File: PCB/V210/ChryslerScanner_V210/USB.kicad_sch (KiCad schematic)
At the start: 11 parts

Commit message: Completed schematic.
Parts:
- gave numbers to parts that had none: 11
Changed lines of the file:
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@@
   (symbol (lib_id "Device:R") (at 180.34 62.23 0) (unit 1)
     (in_bom yes) (on_board yes) (fields_autoplaced)
-    (property "Reference" "R?" (id 0) (at 182.88 60.9599 0)
+    (property "Reference" "R12" (id 0) (at 182.88 60.9599 0)
       (effects (font (size 1.27 1.27)) (justify left))
     )
@@
   (symbol (lib_id "power:PWR_FLAG") (at 88.9 83.82 0) (unit 1)
     (in_bom yes) (on_board yes) (fields_autoplaced)
-    (property "Reference" "#FLG?" (id 0) (at 88.9 81.915 0)
+    (property "Reference" "#FLG01" (id 0) (at 88.9 81.915 0)
       (effects (font (size 1.27 1.27)) hide)
     )
@@
   (symbol (lib_id "power:+3V3") (at 205.74 50.8 0) (unit 1)
     (in_bom yes) (on_board yes) (fields_autoplaced)
-    (property "Reference" "#PWR?" (id 0) (at 205.74 54.61 0)
+    (property "Reference" "#PWR025" (id 0) (at 205.74 54.61 0)
       (effects (font (size 1.27 1.27)) hide)
     )
@@
   (symbol (lib_id "power:+5V") (at 87.63 59.69 0) (unit 1)
     (in_bom yes) (on_board yes) (fields_autoplaced)
-    (property "Reference" "#PWR?" (id 0) (at 87.63 63.5 0)
+    (property "Reference" "#PWR017" (id 0) (at 87.63 63.5 0)
       (effects (font (size 1.27 1.27)) hide)
     )
@@
   (symbol (lib_id "power:VBUS") (at 180.34 50.8 0) (unit 1)
     (in_bom yes) (on_board yes) (fields_autoplaced)
-    (property "Reference" "#PWR?" (id 0) (at 180.34 54.61 0)
+    (property "Reference" "#PWR023" (id 0) (at 180.34 54.61 0)
       (effects (font (size 1.27 1.27)) hide)
     )
@@
   (symbol (lib_id "Interface_USB:CP2102N-Axx-xQFN28") (at 208.28 97.79 0) (unit 1)
     (in_bom yes) (on_board yes) (fields_autoplaced)
-    (property "Reference" "U?" (id 0) (at 210.2994 130.81 0)
+    (property "Reference" "U4" (id 0) (at 210.2994 130.81 0)
       (effects (font (size 1.27 1.27)) (justify left))
     )
@@
   (symbol (lib_id "power:VBUS") (at 120.65 85.09 0) (unit 1)
     (in_bom yes) (on_board yes) (fields_autoplaced)
-    (property "Reference" "#PWR?" (id 0) (at 120.65 88.9 0)
+    (property "Reference" "#PWR019" (id 0) (at 120.65 88.9 0)
       (effects (font (size 1.27 1.27)) hide)
     )
@@
   (symbol (lib_id "power:GND") (at 120.65 139.7 0) (unit 1)
     (in_bom yes) (on_board yes) (fields_autoplaced)
-    (property "Reference" "#PWR?" (id 0) (at 120.65 146.05 0)
+    (property "Reference" "#PWR020" (id 0) (at 120.65 146.05 0)
       (effects (font (size 1.27 1.27)) hide)
     )
@@
   (symbol (lib_id "power:+3V3") (at 165.1 50.8 0) (unit 1)
     (in_bom yes) (on_board yes) (fields_autoplaced)
-    (property "Reference" "#PWR?" (id 0) (at 165.1 54.61 0)
+    (property "Reference" "#PWR021" (id 0) (at 165.1 54.61 0)
       (effects (font (size 1.27 1.27)) hide)
     )
@@
   (symbol (lib_id "Device:R") (at 180.34 76.2 0) (unit 1)
     (in_bom yes) (on_board yes) (fields_autoplaced)
-    (property "Reference" "R?" (id 0) (at 182.88 74.9299 0)
+    (property "Reference" "R13" (id 0) (at 182.88 74.9299 0)
       (effects (font (size 1.27 1.27)) (justify left))
     )
@@
   (symbol (lib_id "Device:R") (at 191.77 62.23 0) (unit 1)
     (in_bom yes) (on_board yes) (fields_autoplaced)
-    (property "Reference" "R?" (id 0) (at 194.31 60.9599 0)
+    (property "Reference" "R14" (id 0) (at 194.31 60.9599 0)
       (effects (font (size 1.27 1.27)) (justify left))
     )
@@
   (symbol (lib_id "Device:C") (at 154.94 59.69 0) (unit 1)
     (in_bom yes) (on_board yes) (fields_autoplaced)
-    (property "Reference" "C?" (id 0) (at 158.75 58.4199 0)
+    (property "Reference" "C14" (id 0) (at 158.75 58.4199 0)
       (effects (font (size 1.27 1.27)) (justify left))
     )
@@
   (symbol (lib_id "power:GND") (at 180.34 82.55 0) (unit 1)
     (in_bom yes) (on_board yes) (fields_autoplaced)
-    (property "Reference" "#PWR?" (id 0) (at 180.34 88.9 0)
+    (property "Reference" "#PWR024" (id 0) (at 180.34 88.9 0)
       (effects (font (size 1.27 1.27)) hide)
     )
@@
   (symbol (lib_id "Power_Protection:USBLC6-2SC6") (at 120.65 101.6 0) (unit 1)
     (in_bom yes) (on_board yes) (fields_autoplaced)
-    (property "Reference" "U?" (id 0) (at 123.4187 88.9 0)
+    (property "Reference" "U3" (id 0) (at 123.4187 88.9 0)
       (effects (font (size 1.27 1.27)) (justify left))
     )
@@
   (symbol (lib_id "Device:D") (at 97.79 63.5 0) (unit 1)
     (in_bom yes) (on_board yes)
-    (property "Reference" "D?" (id 0) (at 97.79 59.69 0))
+    (property "Reference" "D1" (id 0) (at 97.79 59.69 0))
     (property "Value" "MBR0520LT1G" (id 1) (at 97.79 67.31 0))
     (property "Footprint" "" (id 2) (at 97.79 63.5 0)
@@
   (symbol (lib_id "Device:C") (at 165.1 59.69 0) (unit 1)
     (in_bom yes) (on_board yes) (fields_autoplaced)
-    (property "Reference" "C?" (id 0) (at 168.91 58.4199 0)
+    (property "Reference" "C15" (id 0) (at 168.91 58.4199 0)
       (effects (font (size 1.27 1.27)) (justify left))
     )
@@
   (symbol (lib_id "power:GND") (at 165.1 68.58 0) (unit 1)
     (in_bom yes) (on_board yes) (fields_autoplaced)
-    (property "Reference" "#PWR?" (id 0) (at 165.1 74.93 0)
+    (property "Reference" "#PWR022" (id 0) (at 165.1 74.93 0)
       (effects (font (size 1.27 1.27)) hide)
     )
@@
   (symbol (lib_id "Device:FerriteBead_Small") (at 96.52 100.33 0) (mirror x) (unit 1)
     (in_bom yes) (on_board yes) (fields_autoplaced)
-    (property "Reference" "FB?" (id 0) (at 93.98 99.098 0)
+    (property "Reference" "FB1" (id 0) (at 93.98 99.098 0)
       (effects (font (size 1.27 1.27)) (justify right))
     )
@@
   (symbol (lib_id "Device:C") (at 67.31 123.19 0) (unit 1)
     (in_bom yes) (on_board yes) (fields_autoplaced)
-    (property "Reference" "C?" (id 0) (at 71.12 121.9199 0)
+    (property "Reference" "C13" (id 0) (at 71.12 121.9199 0)
       (effects (font (size 1.27 1.27)) (justify left))
     )
@@
   (symbol (lib_id "power:VBUS") (at 107.95 59.69 0) (unit 1)
     (in_bom yes) (on_board yes) (fields_autoplaced)
-    (property "Reference" "#PWR?" (id 0) (at 107.95 63.5 0)
+    (property "Reference" "#PWR018" (id 0) (at 107.95 63.5 0)
       (effects (font (size 1.27 1.27)) hide)
     )
@@
   (symbol (lib_id "Connector:USB_B_Micro") (at 85.09 120.65 0) (unit 1)
     (in_bom yes) (on_board yes) (fields_autoplaced)
-    (property "Reference" "J?" (id 0) (at 85.09 107.95 0))
+    (property "Reference" "J2" (id 0) (at 85.09 107.95 0))
     (property "Value" "USB_B_Micro" (id 1) (at 85.09 110.49 0))
     (property "Footprint" "" (id 2) (at 88.9 121.92 0)
@@
   (symbol (lib_id "power:GND") (at 208.28 140.97 0) (unit 1)
     (in_bom yes) (on_board yes) (fields_autoplaced)
-    (property "Reference" "#PWR?" (id 0) (at 208.28 147.32 0)
-      (effects (font (size 1.27 1.27)) hide)
-    )
+    (property "Reference" "#PWR026" (id 0) (at 208.28 147.32 0)
+      (effects (font (size 1.27 1.27)) hide)
+    )

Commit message: WIP
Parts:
- C13, C14, C15: footprint (none) -> Capacitor_SMD:C_0603_1608Metric
- D1: footprint (none) -> Britishideas:SOD-123
- FB1: footprint (none) -> Resistor_SMD:R_0805_2012Metric; manf# (none) -> MI0805K400R-10
- J1: renamed from J2; footprint (none) -> Connector_USB:USB_Micro-B_Amphenol_10103594-0001LF_Horizontal; manf# (none) -> 10103594-0001LF
- R10: renamed from R12; footprint (none) -> Resistor_SMD:R_0603_1608Metric
- R11: renamed from R13; footprint (none) -> Resistor_SMD:R_0603_1608Metric
- R12: renamed from R14; footprint (none) -> Resistor_SMD:R_0603_1608Metric
- U3: manf# (none) -> USBLC6-2SC6
- U4: manf# (none) -> CP2102N-A02-GQFN28
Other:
- title: Chrysler Scanner -> TJ Diag
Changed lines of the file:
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@@
   (paper "A4")
   (title_block
-    (title "Chrysler Scanner")
-    (date "2023-06-25")
-    (rev "V2.11")
+    (title "TJ Diag")
+    (date "2023-07-01")
+    (rev "V1.00")
     (company "andy@britishideas.com")
     (comment 1 "V210/ChryslerScanner_V210/schematic/ChryslerScanner_V210_schematic.pdf")
@@
   (symbol (lib_id "Device:R") (at 180.34 62.23 0) (unit 1)
     (in_bom yes) (on_board yes) (fields_autoplaced)
-    (property "Reference" "R12" (id 0) (at 182.88 60.9599 0)
+    (property "Reference" "R10" (id 0) (at 182.88 60.9599 0)
       (effects (font (size 1.27 1.27)) (justify left))
     )
@@
       (effects (font (size 1.27 1.27)) (justify left))
     )
-    (property "Footprint" "" (id 2) (at 178.562 62.23 90)
+    (property "Footprint" "Resistor_SMD:R_0603_1608Metric" (id 2) (at 178.562 62.23 90)
       (effects (font (size 1.27 1.27)) hide)
     )
@@
   (symbol (lib_id "power:+3V3") (at 205.74 50.8 0) (unit 1)
     (in_bom yes) (on_board yes) (fields_autoplaced)
-    (property "Reference" "#PWR025" (id 0) (at 205.74 54.61 0)
+    (property "Reference" "#PWR021" (id 0) (at 205.74 54.61 0)
       (effects (font (size 1.27 1.27)) hide)
     )
@@
   (symbol (lib_id "power:+5V") (at 87.63 59.69 0) (unit 1)
     (in_bom yes) (on_board yes) (fields_autoplaced)
-    (property "Reference" "#PWR017" (id 0) (at 87.63 63.5 0)
+    (property "Reference" "#PWR013" (id 0) (at 87.63 63.5 0)
       (effects (font (size 1.27 1.27)) hide)
     )
@@
   (symbol (lib_id "power:VBUS") (at 180.34 50.8 0) (unit 1)
     (in_bom yes) (on_board yes) (fields_autoplaced)
-    (property "Reference" "#PWR023" (id 0) (at 180.34 54.61 0)
+    (property "Reference" "#PWR019" (id 0) (at 180.34 54.61 0)
       (effects (font (size 1.27 1.27)) hide)
     )
@@
     )
     (property "Datasheet" "https://www.silabs.com/documents/public/data-sheets/cp2102n-datasheet.pdf" (id 3) (at 209.55 116.84 0)
+      (effects (font (size 1.27 1.27)) hide)
+    )
+    (property "manf#" "CP2102N-A02-GQFN28" (id 4) (at 208.28 97.79 0)
       (effects (font (size 1.27 1.27)) hide)
     )
@@
   (symbol (lib_id "power:VBUS") (at 120.65 85.09 0) (unit 1)
     (in_bom yes) (on_board yes) (fields_autoplaced)
-    (property "Reference" "#PWR019" (id 0) (at 120.65 88.9 0)
+    (property "Reference" "#PWR015" (id 0) (at 120.65 88.9 0)
       (effects (font (size 1.27 1.27)) hide)
     )
@@
   (symbol (lib_id "power:GND") (at 120.65 139.7 0) (unit 1)
     (in_bom yes) (on_board yes) (fields_autoplaced)
-    (property "Reference" "#PWR020" (id 0) (at 120.65 146.05 0)
+    (property "Reference" "#PWR016" (id 0) (at 120.65 146.05 0)
       (effects (font (size 1.27 1.27)) hide)
     )
@@
   (symbol (lib_id "power:+3V3") (at 165.1 50.8 0) (unit 1)
     (in_bom yes) (on_board yes) (fields_autoplaced)
-    (property "Reference" "#PWR021" (id 0) (at 165.1 54.61 0)
+    (property "Reference" "#PWR017" (id 0) (at 165.1 54.61 0)
       (effects (font (size 1.27 1.27)) hide)
     )
@@
   (symbol (lib_id "Device:R") (at 180.34 76.2 0) (unit 1)
     (in_bom yes) (on_board yes) (fields_autoplaced)
-    (property "Reference" "R13" (id 0) (at 182.88 74.9299 0)
+    (property "Reference" "R11" (id 0) (at 182.88 74.9299 0)
       (effects (font (size 1.27 1.27)) (justify left))
     )
@@
       (effects (font (size 1.27 1.27)) (justify left))
     )
-    (property "Footprint" "" (id 2) (at 178.562 76.2 90)
+    (property "Footprint" "Resistor_SMD:R_0603_1608Metric" (id 2) (at 178.562 76.2 90)
       (effects (font (size 1.27 1.27)) hide)
     )
@@
   (symbol (lib_id "Device:R") (at 191.77 62.23 0) (unit 1)
     (in_bom yes) (on_board yes) (fields_autoplaced)
-    (property "Reference" "R14" (id 0) (at 194.31 60.9599 0)
+    (property "Reference" "R12" (id 0) (at 194.31 60.9599 0)
       (effects (font (size 1.27 1.27)) (justify left))
     )
@@
       (effects (font (size 1.27 1.27)) (justify left))
     )
-    (property "Footprint" "" (id 2) (at 189.992 62.23 90)
+    (property "Footprint" "Resistor_SMD:R_0603_1608Metric" (id 2) (at 189.992 62.23 90)
       (effects (font (size 1.27 1.27)) hide)
     )
@@
       (effects (font (size 1.27 1.27)) (justify left))
     )
-    (property "Footprint" "" (id 2) (at 155.9052 63.5 0)
+    (property "Footprint" "Capacitor_SMD:C_0603_1608Metric" (id 2) (at 155.9052 63.5 0)
       (effects (font (size 1.27 1.27)) hide)
     )
@@
   (symbol (lib_id "power:GND") (at 180.34 82.55 0) (unit 1)
     (in_bom yes) (on_board yes) (fields_autoplaced)
-    (property "Reference" "#PWR024" (id 0) (at 180.34 88.9 0)
+    (property "Reference" "#PWR020" (id 0) (at 180.34 88.9 0)
       (effects (font (size 1.27 1.27)) hide)
     )
@@
     )
     (property "Datasheet" "https://www.st.com/resource/en/datasheet/usblc6-2.pdf" (id 3) (at 125.73 92.71 0)
+      (effects (font (size 1.27 1.27)) hide)
+    )
+    (property "manf#" "USBLC6-2SC6" (id 4) (at 120.65 101.6 0)
       (effects (font (size 1.27 1.27)) hide)
     )
@@
     (property "Reference" "D1" (id 0) (at 97.79 59.69 0))
     (property "Value" "MBR0520LT1G" (id 1) (at 97.79 67.31 0))
-    (property "Footprint" "" (id 2) (at 97.79 63.5 0)
+    (property "Footprint" "Britishideas:SOD-123" (id 2) (at 97.79 63.5 0)
       (effects (font (size 1.27 1.27)) hide)
     )
@@
       (effects (font (size 1.27 1.27)) (justify left))
     )
-    (property "Footprint" "" (id 2) (at 166.0652 63.5 0)
+    (property "Footprint" "Capacitor_SMD:C_0603_1608Metric" (id 2) (at 166.0652 63.5 0)
       (effects (font (size 1.27 1.27)) hide)
     )
@@
   (symbol (lib_id "power:GND") (at 165.1 68.58 0) (unit 1)
     (in_bom yes) (on_board yes) (fields_autoplaced)
-    (property "Reference" "#PWR022" (id 0) (at 165.1 74.93 0)
+    (property "Reference" "#PWR018" (id 0) (at 165.1 74.93 0)
       (effects (font (size 1.27 1.27)) hide)
     )
@@
       (effects (font (size 1.27 1.27)) (justify right))
     )
-    (property "Footprint" "" (id 2) (at 94.742 100.33 90)
+    (property "Footprint" "Resistor_SMD:R_0805_2012Metric" (id 2) (at 94.742 100.33 90)
       (effects (font (size 1.27 1.27)) hide)
     )
@@
       (effects (font (size 1.27 1.27)) hide)
     )
+    (property "manf#" "MI0805K400R-10" (id 4) (at 96.52 100.33 0)
+      (effects (font (size 1.27 1.27)) hide)
+    )
     (pin "1")
     (pin "2")
@@
       (effects (font (size 1.27 1.27)) (justify left))
     )
-    (property "Footprint" "" (id 2) (at 68.2752 127 0)
+    (property "Footprint" "Capacitor_SMD:C_0603_1608Metric" (id 2) (at 68.2752 127 0)
       (effects (font (size 1.27 1.27)) hide)
     )
@@
   (symbol (lib_id "power:VBUS") (at 107.95 59.69 0) (unit 1)
     (in_bom yes) (on_board yes) (fields_autoplaced)
-    (property "Reference" "#PWR018" (id 0) (at 107.95 63.5 0)
+    (property "Reference" "#PWR014" (id 0) (at 107.95 63.5 0)
       (effects (font (size 1.27 1.27)) hide)
     )
@@
   (symbol (lib_id "Connector:USB_B_Micro") (at 85.09 120.65 0) (unit 1)
     (in_bom yes) (on_board yes) (fields_autoplaced)
-    (property "Reference" "J2" (id 0) (at 85.09 107.95 0))
+    (property "Reference" "J1" (id 0) (at 85.09 107.95 0))
     (property "Value" "USB_B_Micro" (id 1) (at 85.09 110.49 0))
-    (property "Footprint" "" (id 2) (at 88.9 121.92 0)
+    (property "Footprint" "Connector_USB:USB_Micro-B_Amphenol_10103594-0001LF_Horizontal" (id 2) (at 88.9 121.92 0)
       (effects (font (size 1.27 1.27)) hide)
     )
     (property "Datasheet" "~" (id 3) (at 88.9 121.92 0)
+      (effects (font (size 1.27 1.27)) hide)
+    )
+    (property "manf#" "10103594-0001LF" (id 4) (at 85.09 120.65 0)
       (effects (font (size 1.27 1.27)) hide)
     )
@@
   (symbol (lib_id "power:GND") (at 208.28 140.97 0) (unit 1)
     (in_bom yes) (on_board yes) (fields_autoplaced)
-    (property "Reference" "#PWR026" (id 0) (at 208.28 147.32 0)
-      (effects (font (size 1.27 1.27)) hide)
-    )
+    (property "Reference" "#PWR022" (id 0) (at 208.28 147.32 0)
+      (effects (font (size 1.27 1.27)) hide)
+    )

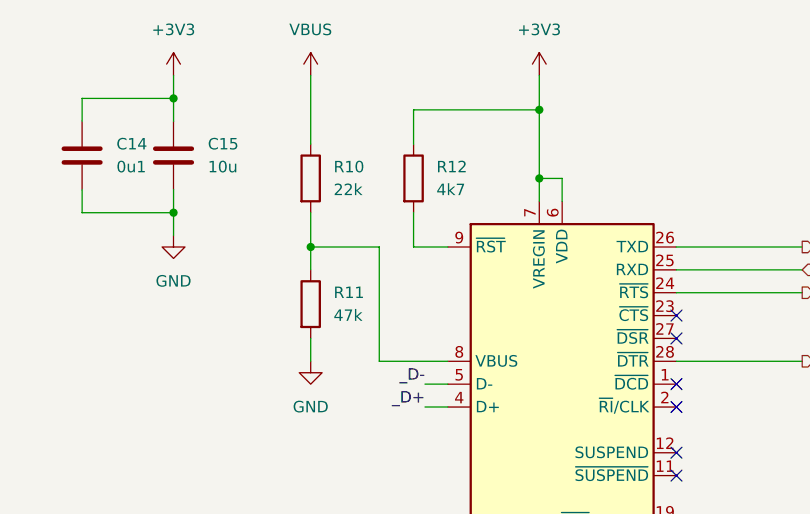
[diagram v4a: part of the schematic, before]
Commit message: Added CCD back in - needed for early TJs.
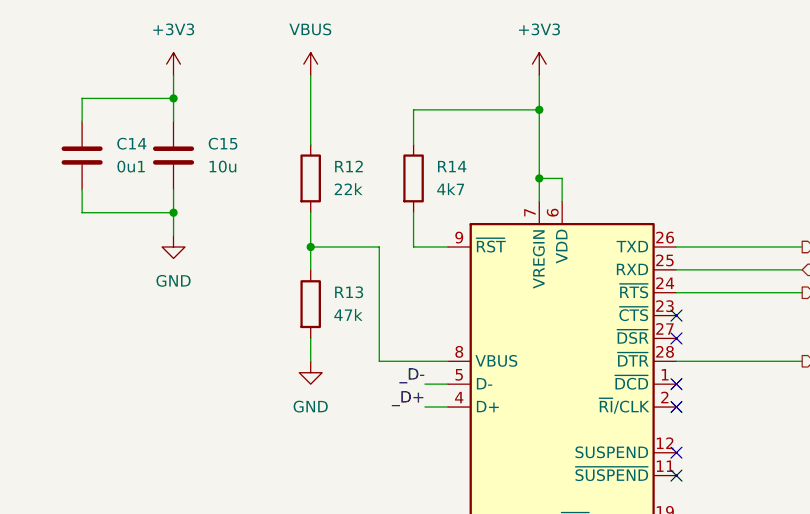
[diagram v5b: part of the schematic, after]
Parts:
- renumbered R10 to R12, R11 to R13, R12 to R14
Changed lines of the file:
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@@
   (title_block
     (title "TJ Diag")
-    (date "2023-07-06")
+    (date "2023-07-07")
     (rev "V1.00")
     (company "andy@britishideas.com")
@@
   (symbol (lib_id "Device:R") (at 180.34 62.23 0) (unit 1)
     (in_bom yes) (on_board yes) (fields_autoplaced)
-    (property "Reference" "R10" (id 0) (at 182.88 60.9599 0)
+    (property "Reference" "R12" (id 0) (at 182.88 60.9599 0)
       (effects (font (size 1.27 1.27)) (justify left))
     )
@@
   (symbol (lib_id "Device:R") (at 180.34 76.2 0) (unit 1)
     (in_bom yes) (on_board yes) (fields_autoplaced)
-    (property "Reference" "R11" (id 0) (at 182.88 74.9299 0)
+    (property "Reference" "R13" (id 0) (at 182.88 74.9299 0)
       (effects (font (size 1.27 1.27)) (justify left))
     )
@@
   (symbol (lib_id "Device:R") (at 191.77 62.23 0) (unit 1)
     (in_bom yes) (on_board yes) (fields_autoplaced)
-    (property "Reference" "R12" (id 0) (at 194.31 60.9599 0)
-      (effects (font (size 1.27 1.27)) (justify left))
-    )
+    (property "Reference" "R14" (id 0) (at 194.31 60.9599 0)
+      (effects (font (size 1.27 1.27)) (justify left))
+    )
